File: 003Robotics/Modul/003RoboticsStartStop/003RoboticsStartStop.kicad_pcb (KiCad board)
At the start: 4 copper layers, 12 x 11 mm, 16 parts, among them J1 Conn_ARM_SWD_TagConnect_TC203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, J2 I/O Header, U2 TSOP392, U3 STM32C011F4, U4 LDK220PU33R

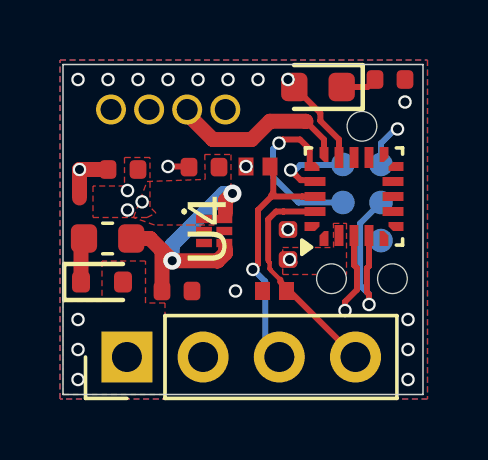
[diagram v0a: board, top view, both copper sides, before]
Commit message: Inverted SWDIO/SWCLK to correct pins.
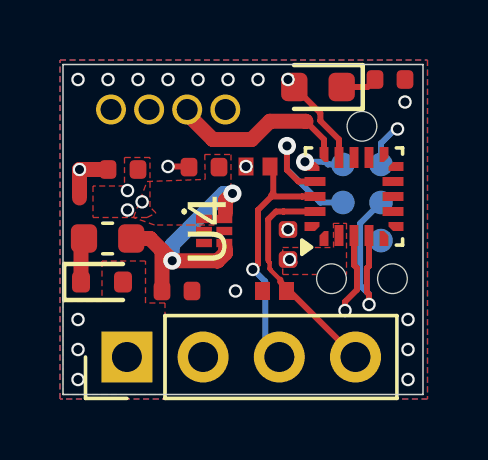
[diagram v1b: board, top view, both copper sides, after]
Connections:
- U3 pad 16: /SWCLK -> /SWDATA
- U3 pad 17: /SWDATA -> /SWCLK
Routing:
- net /SWDATA: track 2.82 -> 1.80 mm
- net /SWCLK: track 5.89 -> 5.00 mm
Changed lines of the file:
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@@
 			(size 0.3 0.35)
 			(layers "F.Cu" "F.Mask" "F.Paste")
-			(net 13 "/SWCLK")
+			(net 11 "/SWDATA")
 			(pinfunction "PA13")
 			(pintype "bidirectional")
@@
 			(size 0.3 0.7)
 			(layers "F.Cu" "F.Mask" "F.Paste")
-			(net 11 "/SWDATA")
+			(net 13 "/SWCLK")
 			(pinfunction "PA14")
 			(pintype "bidirectional")
@@
 	)
 	(segment
-		(start 134.9 87.355999)
-		(end 134.9 87.4)
+		(start 134.725 86.899999)
+		(end 134.775258 86.849741)
 		(width 0.2)
 		(layer "F.Cu")
@@
 	)
 	(segment
-		(start 134.244 87.171762)
-		(end 134.244 87.176751)
+		(start 134.775258 86.849741)
+		(end 134.848682 86.849741)
 		(width 0.2)
 		(layer "F.Cu")
@@
 	)
 	(segment
-		(start 134.089442 87.017204)
-		(end 134.244 87.171762)
+		(start 134.568539 86.743538)
+		(end 134.725 86.899999)
 		(width 0.2)
 		(layer "F.Cu")
@@
 	)
 	(segment
-		(start 134.244 87.176751)
-		(end 134.423248 87.355999)
+		(start 134.566047 86.743538)
+		(end 134.568539 86.743538)
 		(width 0.2)
 		(layer "F.Cu")
@@
 	)
 	(segment
-		(start 134.423248 87.355999)
-		(end 134.9 87.355999)
+		(start 134.848682 86.849741)
+		(end 134.89894 86.899999)
 		(width 0.2)
 		(layer "F.Cu")
@@
 	)
 	(via
-		(at 134.089442 87.017204)
-		(size 0.45)
+		(at 134.566047 86.743538)
+		(size 0.6)
 		(drill 0.3)
 		(layers "F.Cu" "B.Cu")
@@
 	)
 	(segment
-		(start 134.240199 87.017204)
-		(end 134.407769 86.849634)
+		(start 134.566047 86.743538)
+		(end 135.198946 86.743538)
 		(width 0.2)
 		(layer "B.Cu")
@@
 	)
 	(segment
-		(start 134.407769 86.849634)
-		(end 135.810367 86.849634)
+		(start 135.198946 86.698946)
+		(end 135.33 86.83)
 		(width 0.2)
 		(layer "B.Cu")
@@
 	)
 	(segment
-		(start 134.089442 87.017204)
-		(end 134.240199 87.017204)
+		(start 135.33 86.83)
+		(end 135.830001 86.83)
 		(width 0.2)
 		(layer "B.Cu")
@@
 	)
 	(segment
-		(start 135.810367 86.849634)
-		(end 135.830001 86.83)
+		(start 135.198946 86.743538)
+		(end 135.198946 86.698946)
 		(width 0.2)
 		(layer "B.Cu")
@@
 	)
 	(segment
-		(start 133.821356 86)
-		(end 134.400001 86)
+		(start 134.35 87.4)
+		(end 133.965047 87.015047)
 		(width 0.2)
 		(layer "F.Cu")
@@
 	)
 	(segment
-		(start 133.699147 86.122209)
-		(end 133.821356 86)
+		(start 133.965047 86.215228)
+		(end 133.966969 86.213306)
 		(width 0.2)
 		(layer "F.Cu")
@@
 	)
 	(segment
-		(start 134.725 86.899999)
-		(end 134.775258 86.849741)
+		(start 133.965047 87.015047)
+		(end 133.965047 86.215228)
 		(width 0.2)
 		(layer "F.Cu")
@@
 	)
 	(segment
-		(start 134.775258 86.849741)
-		(end 134.848682 86.849741)
+		(start 134.9 87.4)
+		(end 134.35 87.4)
 		(width 0.2)
 		(layer "F.Cu")
 		(net 13)
 	)
-	(segment
-		(start 134.848682 86.849741)
-		(end 134.89894 86.899999)
-		(width 0.2)
-		(layer "F.Cu")
+	(via
+		(at 133.966969 86.213306)
+		(size 0.6)
+		(drill 0.3)
+		(layers "F.Cu" "B.Cu")
 		(net 13)
 	)
 	(segment
-		(start 134.400001 86)
-		(end 134.725 86.324999)
-		(width 0.2)
-		(layer "F.Cu")
+		(start 133.966969 86.213306)
+		(end 133.965047 86.215228)
+		(width 0.2)
+		(layer "B.Cu")
 		(net 13)
 	)
 	(segment
-		(start 134.725 86.324999)
-		(end 134.725 86.899999)
-		(width 0.2)
-		(layer "F.Cu")
+		(start 135.072566 88.1)
+		(end 135.83 88.1)
+		(width 0.2)
+		(layer "B.Cu")
 		(net 13)
 	)
-	(via
-		(at 133.699147 86.122209)
-		(size 0.45)
-		(drill 0.3)
-		(layers "F.Cu" "B.Cu")
+	(segment
+		(start 133.965047 86.992481)
+		(end 135.072566 88.1)
+		(width 0.2)
+		(layer "B.Cu")
 		(net 13)
 	)
 	(segment
-		(start 133.5 86.321356)
-		(end 133.5 87.25)
-		(width 0.2)
-		(layer "B.Cu")
-		(net 13)
-	)
-	(segment
-		(start 133.5 87.25)
-		(end 134.35 88.1)
-		(width 0.2)
-		(layer "B.Cu")
-		(net 13)
-	)
-	(segment
-		(start 133.699147 86.122209)
-		(end 133.5 86.321356)
-		(width 0.2)
-		(layer "B.Cu")
-		(net 13)
-	)
-	(segment
-		(start 134.35 88.1)
-		(end 135.83 88.1)
-		(width 0.2)
-		(layer "B.Cu")
+		(start 133.965047 86.215228)
+		(end 133.965047 86.992481)
+		(width 0.2)
+		(layer "B.Cu")
